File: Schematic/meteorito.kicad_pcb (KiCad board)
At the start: 2 copper layers, 95.3 x 89.4 mm, 19 parts, among them P1 DH22, P10 CONN_01X10, P2 GY-ML8511, P3 BMP180, P4 Hall, P5 Hall, P6 Hall, P7 CONN_01X10, P8 CONN_01X10, P9 CONN_01X10

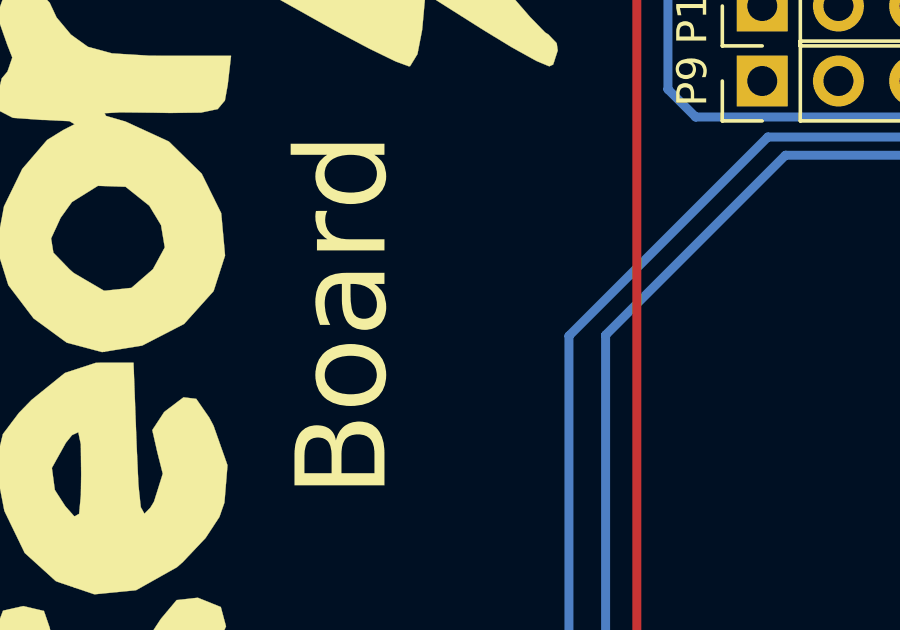
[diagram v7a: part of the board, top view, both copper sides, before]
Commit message: Remove NC pins
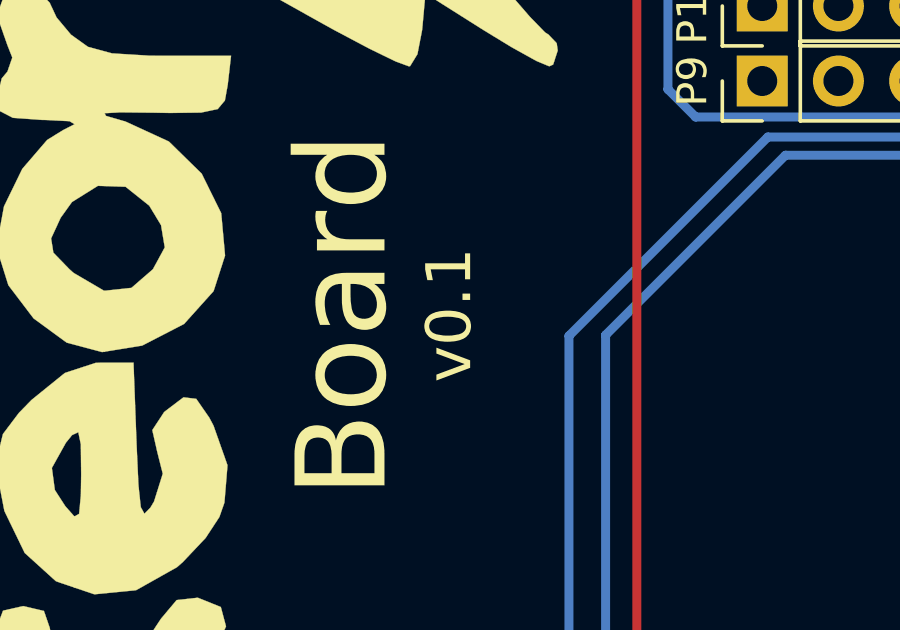
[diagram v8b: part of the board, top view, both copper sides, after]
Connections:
- P10 pad 2: /NC -> Net-(P10-Pad2)
- P10 pad 8: /NC -> Net-(P10-Pad8)
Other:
- board text added: "v0.1"
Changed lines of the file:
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@@
-(kicad_pcb (version 20171130) (host pcbnew "(5.0.0)")
+(kicad_pcb (version 20171130) (host pcbnew "(5.0.0-3-g5ebb6b6)")
   (general
     (thickness 1.6)
-    (drawings 32)
+    (drawings 33)
     (tracks 144)
     (zones 0)
     (modules 19)
-    (nets 39)
+    (nets 40)
   )
   (page A4)
+  (title_block
+    (title "Meteorito Board")
+    (date 2018-11-12)
+    (rev 0.1)
+    (company "Electronic Cats")
+    (comment 1 "Diego Armadillo")
+    (comment 2 "Andres Sabas")
+  )
   (layers
     (0 F.Cu signal)
@@
   (net 29 /CMD)
   (net 30 /SD2)
-  (net 31 /NC)
-  (net 32 /TMS)
-  (net 33 /IO34)
-  (net 34 /IO33)
-  (net 35 /IO35)
-  (net 36 /SVN)
-  (net 37 +3V3)
-  (net 38 /IO13)
+  (net 31 /TMS)
+  (net 32 /IO34)
+  (net 33 /IO33)
+  (net 34 /IO35)
+  (net 35 /SVN)
+  (net 36 +3V3)
+  (net 37 /IO13)
+  (net 38 "Net-(P10-Pad8)")
+  (net 39 "Net-(P10-Pad2)")
   (net_class Default "Esta es la clase de red por defecto."
     (clearance 0.2)
@@
     (add_net /IO4)
     (add_net /IO5)
-    (add_net /NC)
     (add_net /RST)
     (add_net /RXD)
@@
     (add_net /TXD)
     (add_net GND)
+    (add_net "Net-(P10-Pad2)")
+    (add_net "Net-(P10-Pad8)")
     (add_net "Net-(P2-Pad2)")
     (add_net "Net-(P7-Pad7)")
@@
       (net 27 /IO5))
     (pad 8 thru_hole oval (at 0 17.78 90) (size 1.7 1.7) (drill 1) (layers *.Cu *.Mask)
-      (net 37 +3V3))
+      (net 36 +3V3))
     (pad 9 thru_hole oval (at 0 20.32 90) (size 1.7 1.7) (drill 1) (layers *.Cu *.Mask)
-      (net 38 /IO13))
+      (net 37 /IO13))
     (pad 10 thru_hole oval (at 0 22.86 90) (size 1.7 1.7) (drill 1) (layers *.Cu *.Mask)
       (net 28 /SD3))
@@
       (net 30 /SD2))
     (pad 8 thru_hole oval (at 0 17.78 90) (size 1.7 1.7) (drill 1) (layers *.Cu *.Mask)
-      (net 31 /NC))
+      (net 38 "Net-(P10-Pad8)"))
     (pad 7 thru_hole oval (at 0 15.24 90) (size 1.7 1.7) (drill 1) (layers *.Cu *.Mask)
-      (net 32 /TMS))
+      (net 31 /TMS))
     (pad 6 thru_hole oval (at 0 12.7 90) (size 1.7 1.7) (drill 1) (layers *.Cu *.Mask)
-      (net 33 /IO34))
+      (net 32 /IO34))
     (pad 5 thru_hole oval (at 0 10.16 90) (size 1.7 1.7) (drill 1) (layers *.Cu *.Mask)
-      (net 34 /IO33))
+      (net 33 /IO33))
     (pad 4 thru_hole oval (at 0 7.62 90) (size 1.7 1.7) (drill 1) (layers *.Cu *.Mask)
-      (net 35 /IO35))
+      (net 34 /IO35))
     (pad 3 thru_hole oval (at 0 5.08 90) (size 1.7 1.7) (drill 1) (layers *.Cu *.Mask)
-      (net 36 /SVN))
+      (net 35 /SVN))
     (pad 2 thru_hole oval (at 0 2.54 90) (size 1.7 1.7) (drill 1) (layers *.Cu *.Mask)
-      (net 31 /NC))
+      (net 39 "Net-(P10-Pad2)"))
     (pad 1 thru_hole rect (at 0 0 90) (size 1.7 1.7) (drill 1) (layers *.Cu *.Mask)
       (net 4 GND))
@@
     )
     (pad 1 thru_hole circle (at 0 0) (size 1.4 1.4) (drill 0.7) (layers *.Cu *.Mask)
-      (net 37 +3V3))
+      (net 36 +3V3))
     (pad 2 thru_hole oval (at 2.54 0) (size 1.4 1.4) (drill 0.7) (layers *.Cu *.Mask)
-      (net 38 /IO13))
+      (net 37 /IO13))
     (model ${KISYS3DMOD}/Resistor_THT.3dshapes/R_Axial_DIN0204_L3.6mm_D1.6mm_P2.54mm_Vertical.wrl
       (at (xyz 0 0 0))
@@
     )
     (pad 1 thru_hole circle (at 0 0) (size 1.4 1.4) (drill 0.7) (layers *.Cu *.Mask)
-      (net 38 /IO13))
+      (net 37 /IO13))
     (pad 2 thru_hole oval (at 7.62 0) (size 1.4 1.4) (drill 0.7) (layers *.Cu *.Mask)
       (net 4 GND))
@@
     )
   )
+  (gr_text v0.1 (at 66.65 96.6 90) (layer F.SilkS)
+    (effects (font (size 1.5 1.5) (thickness 0.3)))
+  )
   (dimension 15.039388 (width 0.3) (layer Margin)
     (gr_text "15.039 mm" (at 109.082619 47.213116 0.1451502878) (layer Margin)
@@
   (segment (start 86.28 73.11518) (end 86.28 70.2) (width 0.3) (layer B.Cu) (net 10))
   (segment (start 87.02294 73.85812) (end 86.28 73.11518) (width 0.3) (layer B.Cu) (net 10))
-  (segment (start 75.4 126.010051) (end 75.438 125.972051) (width 0.3) (layer B.Cu) (net 37))
-  (segment (start 75.4 127) (end 75.4 126.010051) (width 0.3) (layer B.Cu) (net 37))
-  (segment (start 75.438 125.972051) (end 75.438 121.08942) (width 0.3) (layer B.Cu) (net 37))
-  (segment (start 75.438 121.08942) (end 74.2823 119.93372) (width 0.3) (layer B.Cu) (net 37))
-  (segment (start 74.2823 119.93372) (end 72.3265 119.93372) (width 0.3) (layer B.Cu) (net 37))
-  (segment (start 72.3265 119.93372) (end 70.6374 118.24462) (width 0.3) (layer B.Cu) (net 37))
-  (segment (start 70.6374 118.24462) (end 70.6374 97.29724) (width 0.3) (layer B.Cu) (net 37))
-  (segment (start 70.6374 97.29724) (end 77.2668 90.66784) (width 0.3) (layer B.Cu) (net 37))
-  (segment (start 77.2668 90.66784) (end 94.29242 90.66784) (width 0.3) (layer B.Cu) (net 37))
-  (segment (start 94.86 90.10026) (end 94.86 88.8) (width 0.3) (layer B.Cu) (net 37))
-  (segment (start 94.29242 90.66784) (end 94.86 90.10026) (width 0.3) (layer B.Cu) (net 37))
-  (segment (start 77.94 127) (end 84.88 127) (width 0.3) (layer F.Cu) (net 38))
-  (segment (start 84.88 126.010051) (end 85.04174 125.848311) (width 0.3) (layer B.Cu) (net 38))
-  (segment (start 84.88 127) (end 84.88 126.010051) (width 0.3) (layer B.Cu) (net 38))
-  (segment (start 85.04174 125.848311) (end 85.04174 121.9708) (width 0.3) (layer B.Cu) (net 38))
-  (segment (start 85.04174 121.9708) (end 81.84134 118.7704) (width 0.3) (layer B.Cu) (net 38))
-  (segment (start 81.84134 118.7704) (end 72.95134 118.7704) (width 0.3) (layer B.Cu) (net 38))
-  (segment (start 72.95134 118.7704) (end 71.85914 117.6782) (width 0.3) (layer B.Cu) (net 38))
-  (segment (start 71.85914 117.6782) (end 71.85914 97.2693) (width 0.3) (layer B.Cu) (net 38))
-  (segment (start 71.85914 97.2693) (end 77.85354 91.2749) (width 0.3) (layer B.Cu) (net 38))
-  (segment (start 77.85354 91.2749) (end 96.81972 91.2749) (width 0.3) (layer B.Cu) (net 38))
-  (segment (start 97.4 90.69462) (end 97.4 88.8) (width 0.3) (layer B.Cu) (net 38))
-  (segment (start 96.81972 91.2749) (end 97.4 90.69462) (width 0.3) (layer B.Cu) (net 38))
+  (segment (start 75.4 126.010051) (end 75.438 125.972051) (width 0.3) (layer B.Cu) (net 36))
+  (segment (start 75.4 127) (end 75.4 126.010051) (width 0.3) (layer B.Cu) (net 36))
+  (segment (start 75.438 125.972051) (end 75.438 121.08942) (width 0.3) (layer B.Cu) (net 36))
+  (segment (start 75.438 121.08942) (end 74.2823 119.93372) (width 0.3) (layer B.Cu) (net 36))
+  (segment (start 74.2823 119.93372) (end 72.3265 119.93372) (width 0.3) (layer B.Cu) (net 36))
+  (segment (start 72.3265 119.93372) (end 70.6374 118.24462) (width 0.3) (layer B.Cu) (net 36))
+  (segment (start 70.6374 118.24462) (end 70.6374 97.29724) (width 0.3) (layer B.Cu) (net 36))
+  (segment (start 70.6374 97.29724) (end 77.2668 90.66784) (width 0.3) (layer B.Cu) (net 36))
+  (segment (start 77.2668 90.66784) (end 94.29242 90.66784) (width 0.3) (layer B.Cu) (net 36))
+  (segment (start 94.86 90.10026) (end 94.86 88.8) (width 0.3) (layer B.Cu) (net 36))
+  (segment (start 94.29242 90.66784) (end 94.86 90.10026) (width 0.3) (layer B.Cu) (net 36))
+  (segment (start 77.94 127) (end 84.88 127) (width 0.3) (layer F.Cu) (net 37))
+  (segment (start 84.88 126.010051) (end 85.04174 125.848311) (width 0.3) (layer B.Cu) (net 37))
+  (segment (start 84.88 127) (end 84.88 126.010051) (width 0.3) (layer B.Cu) (net 37))
+  (segment (start 85.04174 125.848311) (end 85.04174 121.9708) (width 0.3) (layer B.Cu) (net 37))
+  (segment (start 85.04174 121.9708) (end 81.84134 118.7704) (width 0.3) (layer B.Cu) (net 37))
+  (segment (start 81.84134 118.7704) (end 72.95134 118.7704) (width 0.3) (layer B.Cu) (net 37))
+  (segment (start 72.95134 118.7704) (end 71.85914 117.6782) (width 0.3) (layer B.Cu) (net 37))
+  (segment (start 71.85914 117.6782) (end 71.85914 97.2693) (width 0.3) (layer B.Cu) (net 37))
+  (segment (start 71.85914 97.2693) (end 77.85354 91.2749) (width 0.3) (layer B.Cu) (net 37))
+  (segment (start 77.85354 91.2749) (end 96.81972 91.2749) (width 0.3) (layer B.Cu) (net 37))
+  (segment (start 97.4 90.69462) (end 97.4 88.8) (width 0.3) (layer B.Cu) (net 37))
+  (segment (start 96.81972 91.2749) (end 97.4 90.69462) (width 0.3) (layer B.Cu) (net 37))
   (zone (net 4) (net_name GND) (layer F.Cu) (hatch edge 0.508)
     (connect_pads (clearance 0.508))
